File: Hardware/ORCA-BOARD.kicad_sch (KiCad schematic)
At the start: 23 parts, among them J1 USB_C_Receptacle_USB2.0_16P, J3 Screw_Terminal_01x02, SW1 RESET1, SW2 BOOT, U1 D3V3XA4B10LP, U2 ESP32-S3-WROOM-1, U3 AMS1117-3.3, U4 TCA9548APWR

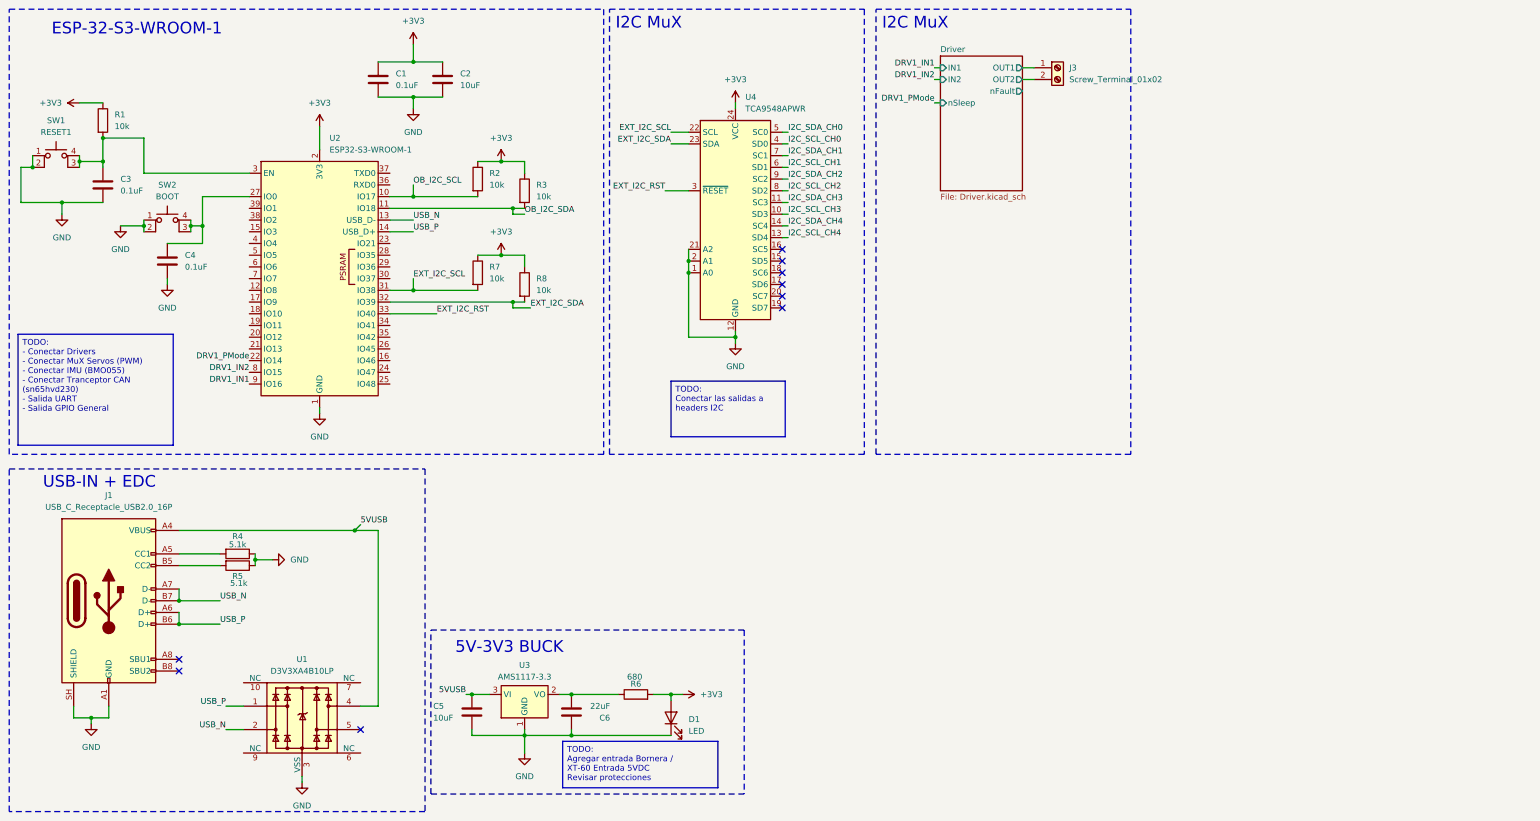
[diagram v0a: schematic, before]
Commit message: Placa de potencia: layout Rev A ruteado y conectado
Buck-boost sincrono de 4 interruptores (LM5175PWPR + 4x PSMN3R2-40YLD) que
entrega 7.2-25 V ajustables a 8 A continuos / 15 A pico desde un pack LiPo
2S-6S, para alimentar los 4 DRV8874.

Layout
- 4 capas, 67.0 x 51.4 mm, 47 componentes, 32 redes, todo SMD en F.Cu
- Ruteo completo: 0 unconnected items
- Corriente de potencia por planos: VBUS, VOUT, VOUT_PRE, SW1 y SW2 con pour
  en F.Cu + In1 + In2 en vez de pistas anchas
- 132 vias de cosido: 16 en SW1, 16 en SW2, 21 en VOUT, 19 en VBUS, 13 en
  VOUT_PRE. Dimensionadas por cantidad, no por tamano
- Vias 0.4/0.3 mm, piso de fabricacion de JLCPCB (recomendacion de Jorge
  Montes). min_via_annular_width ajustado de 0.1 a 0.05 mm para reflejar la
  capacidad real de la fabrica en vez de una regla heredada
- Plano de GND en In1 a 0.1 mm bajo la etapa de potencia, GND y GNDA
  separadas con punto unico de union en R15 (jumper 0 ohm)
- Escape fino (neck-down 0.08 mm) en los pines de U1 donde el paso de
  0.65 mm no admite el clearance de la netclass vecina

Correcciones de netlist
- CS_P/CS_N: el renombrado parcial del lado de U1 dejaba redes de un solo pad
  y el sensado de corriente fisicamente desconectado
- D1: la cadena de bias VBUS -> D1 -> R1 -> VIN colgaba de VCC, que U1 genera
  a partir de VIN. Lazo cerrado sin fuente

Se elimina Hardware/Driver.kicad_sch: el subsheet de drivers pertenece a la
placa logica y el esquematico de potencia ya no lo referencia.

Pendiente antes de fabricar
- Re-exportar Gerbers (los versionados aqui son del 24-sep y no reflejan
  este trabajo)
- Correr DRC sobre esta version y habilitar el parity check con el esquematico
- Verificar la polaridad de ISNS contra el datasheet
- Confirmar continuidad del plano de GND en In1 bajo el lazo de potencia

Detalle completo en Hardware/ORCA-BOARD_Handoff_Ruteo_Manual.md y en
docs/ORCA-Potencia_Dossier_Buck-Boost.md

Co-Authored-By: Claude Opus 5 <noreply@anthropic.com>
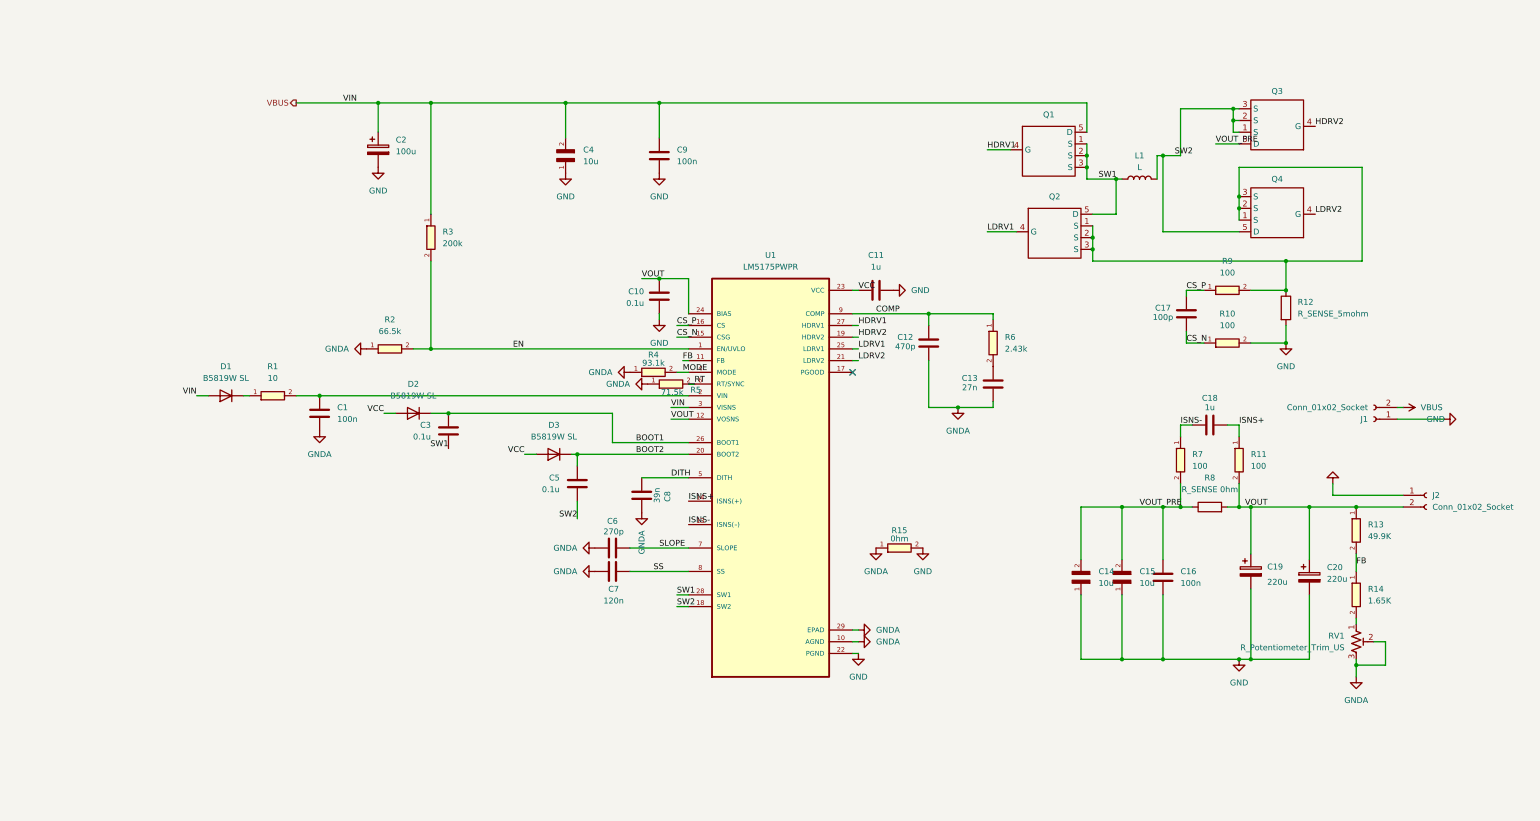
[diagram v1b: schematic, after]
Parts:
- removed C2: 10uF, Capacitor_SMD:C_1206_3216Metric_Pad1.33x1.80mm_HandSolder, symbol Device:C
- removed C4: 0.1uF, Capacitor_SMD:C_0603_1608Metric_Pad1.08x0.95mm_HandSolder, symbol Device:C
- removed D1: LED, LED_SMD:LED_0603_1608Metric_Pad1.05x0.95mm_HandSolder, symbol Device:LED
- removed J1: USB_C_Receptacle_USB2.0_16P, symbol Connector:USB_C_Receptacle_USB2.0_16P
- removed J3: Screw_Terminal_01x02, symbol Connector:Screw_Terminal_01x02
- removed R1, R2, R3, R7: 10k, LED_SMD:LED_0603_1608Metric_Pad1.05x0.95mm_HandSolder, symbol Device:R
- removed R4, R5: 5.1k, LED_SMD:LED_0603_1608Metric_Pad1.05x0.95mm_HandSolder, symbol Device:R
- removed R6: 680, LED_SMD:LED_0603_1608Metric_Pad1.05x0.95mm_HandSolder, symbol Device:R
- removed SW1: RESET1, Button_Switch_SMD:SW_MEC_5GSH9, symbol Switch:SW_MEC_5E
- removed SW2: BOOT, Button_Switch_SMD:SW_MEC_5GSH9, symbol Switch:SW_MEC_5E
- removed U1: D3V3XA4B10LP, Package_DFN_QFN:Diodes_UDFN-10_1x2.5mm_P0.5mm, symbol Power_Protection:D3V3XA4B10LP
- removed U2: ESP32-S3-WROOM-1, RF_Module:ESP32-S3-WROOM-1, symbol RF_Module:ESP32-S3-WROOM-1
- removed U3: AMS1117-3.3, Package_TO_SOT_SMD:SOT-223-3_TabPin2, symbol Regulator_Linear:AMS1117-3.3
- removed U4: TCA9548APWR, Package_SO:TSSOP-24_4.4x7.8mm_P0.65mm, symbol Interface_Expansion:TCA9548APWR
- added C10: 0.1u, RC0603FR-1375RL:0603, symbol Device:C
- added C11, C18: 1u, C0805X105K8RAC7210:CAPC2012X100N, symbol Device:C
- added C12: 470p, RC0603FR-1375RL:0603, symbol Device:C
- added C13: 27n, RC0603FR-1375RL:0603, symbol Device:C
- added C14, C15, C4: 10u, CGA6P1X7R1E106M250AC:CAPC3225X280N, symbol CGA6P1X7R1E106M250AC:CGA6P1X7R1E106M250AC
- added C16, C9: 100n, CGA6P1X7R1E106M250AC:CAPC3225X280N, symbol Device:C
- added C17: 100p, RC0603FR-1375RL:0603, symbol Device:C
- added C19, C20: 220u, Capacitor_THT:CP_Radial_D8.0mm_P3.50mm, symbol Device:C_Polarized
- added C2: 100u, Capacitor_THT:CP_Radial_D8.0mm_P3.50mm, symbol Device:C_Polarized
- added C7: 120n, RC0603FR-1375RL:0603, symbol Device:C
- added C8: 39n, RC0603FR-1375RL:0603, symbol Device:C
- added D1, D2, D3: B5819W SL, Diode_SMD:D_SOD-123, symbol Diode:1N4448W
- added J1, J2: Conn_01x02_Socket, Connector_AMASS:AMASS_XT60-F_1x02_P7.20mm_Vertical, symbol Connector:Conn_01x02_Socket
- added L1: L, ORCAVO:L_Pulse_PA4344, symbol Device:L
- added Q1, Q2, Q3, Q4: (no value), Package_TO_SOT_SMD:LFPAK56, symbol LM5175PWPR:PSMN3R2-40YLD
- added R1: 10, RC0603FR-1375RL:0603, symbol RC0603FR-1375RL:R_0603
- added R10, R11, R7, R9: 100, RC0603FR-1375RL:0603, symbol RC0603FR-1375RL:R_0603
- added R12: R_SENSE_5mohm, ORCAVO:R_2512_Kelvin_TLRP, symbol Device:R
- added R13: 49.9K, RC0603FR-1375RL:0603, symbol RC0603FR-1375RL:R_0603
- added R14: 1.65K, RC0603FR-1375RL:0603, symbol RC0603FR-1375RL:R_0603
- added R15: 0hm, RC0603FR-1375RL:0603, symbol RC0603FR-1375RL:R_0603
- added R2: 66.5k, RC0603FR-1375RL:0603, symbol RC0603FR-1375RL:R_0603
- added R3: 200k, RC0603FR-1375RL:0603, symbol RC0603FR-1375RL:R_0603
- added R4: 93.1k, RC0603FR-1375RL:0603, symbol RC0603FR-1375RL:R_0603
- added R5: 71.5k, RC0603FR-1375RL:0603, symbol RC0603FR-1375RL:R_0603
- added R6: 2.43k, RC0603FR-1375RL:0603, symbol RC0603FR-1375RL:R_0603
- added RV1: R_Potentiometer_Trim_US, Potentiometer_THT:Potentiometer_Bourns_3296W_Vertical, symbol Device:R_Potentiometer_Trim_US
- added U1: LM5175PWPR, ORCAVO:LM5175PWP, symbol LM5175PWPR:LM5175PWPR
- C1: value 0.1uF -> 100n; footprint Capacitor_SMD:C_0603_1608Metric_Pad1.08x0.95mm_HandSolder -> RC0603FR-1375RL:0603
- C3: value 0.1uF -> 0.1u; footprint Capacitor_SMD:C_0603_1608Metric_Pad1.08x0.95mm_HandSolder -> RC0603FR-1375RL:0603
- C5: value 10uF -> 0.1u; footprint Capacitor_SMD:C_1206_3216Metric_Pad1.33x1.80mm_HandSolder -> RC0603FR-1375RL:0603
- C6: value 22uF -> 270p; footprint Capacitor_SMD:C_1206_3216Metric_Pad1.33x1.80mm_HandSolder -> RC0603FR-1375RL:0603
- R8: value 10k -> R_SENSE 0hm; footprint LED_SMD:LED_0603_1608Metric_Pad1.05x0.95mm_HandSolder -> 2512_RSENSE:RES_1-2176421-2
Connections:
- net GND: now also C10.2, C11.2, C14.1, C15.1, C16.2, C19.2, C2.2, C20.2, C4.1, C9.2, J1.1 (Pin_1), J2.1 (Pin_1), R10.2, R12.2, R15.2, U1.22 (PGND); no longer C1.2, C3.2, C5.2, C6.1
- net BOOT1: now reaches C3.1
- net BOOT1: now also D2.1 (K), U1.26 (BOOT1)
- net SLOPE: now reaches C6.2
- net SLOPE: now also U1.7 (SLOPE)
- net +3V3: no longer names the net of C1.1
- net +3V3: now also R1.2, U1.2 (VIN); no longer R8.1
- net 5VUSB renamed BOOT2
- net BOOT2: now also D3.1 (K), U1.20 (BOOT2)
- net EXT_I2C_SDA renamed VOUT
- net VOUT: now also C10.1, C19.1, C20.1, J2.2 (Pin_2), R11.2, R13.1, U1.12 (VOSNS), U1.24 (BIAS)
- new net: C13.2, R6.2
- new net: R14.2, RV1.1
- new net: D1.1 (K), R1.1
- new net: Q2.1 (S), Q2.2 (S), Q2.3 (S), Q4.1 (S), Q4.2 (S), Q4.3 (S), R12.1, R9.2
- new net COMP: C12.2, R6.1, U1.9 (COMP)
- new net CS_N: C17.1, R10.1, U1.15 (CSG)
- new net CS_P: C17.2, R9.1, U1.16 (CS)
- new net DITH: C8.2, U1.5 (DITH)
- new net EN: R2.2, R3.2, U1.1 (EN/UVLO)
- new net FB: R13.2, R14.1, U1.11 (FB)
- new net GNDA: C1.2, C12.1, C13.1, C6.1, C7.1, C8.1, R15.1, R2.1, R4.1, R5.1, RV1.2, RV1.3, U1.10 (AGND), U1.29 (EPAD)
- new net HDRV1: Q1.4 (G), U1.27 (HDRV1)
- new net HDRV2: Q3.4 (G), U1.19 (HDRV2)
- new net ISNS+: C18.2, R11.1, U1.14 (ISNS(+))
- new net ISNS-: C18.1, R7.1, U1.13 (ISNS(–))
- new net LDRV1: Q2.4 (G), U1.25 (LDRV1)
- new net LDRV2: Q4.4 (G), U1.21 (LDRV2)
- new net MODE: R4.2, U1.4 (MODE)
- new net RT: R5.2, U1.6 (RT/SYNC)
- new net SS: C7.2, U1.8 (SS)
- new net SW1: C3.2, L1.1, Q1.1 (S), Q1.2 (S), Q1.3 (S), Q2.5 (D), U1.28 (SW1)
- new net SW2: C5.2, L1.2, Q3.1 (S), Q3.2 (S), Q3.3 (S), Q4.5 (D), U1.18 (SW2)
- new net VBUS: C2.1, C4.2, C9.1, D1.2 (A), J1.2 (Pin_2), Q1.5 (D), R3.1, U1.3 (VISNS)
- new net VCC: C11.1, D2.2 (A), D3.2 (A), U1.23 (VCC)
- new net VOUT_PRE: C14.2, C15.2, C16.1, Q3.5 (D), R7.2, R8.1
- no-connect marks 9 -> 1
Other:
- removed sheet Driver
- note removed: "5V-3V3 BUCK"
- note removed: "ESP-32-S3-WROOM-1"
- note removed: "I2C MuX"
- note removed: "USB-IN + EDC"
- company: (none) -> L.A.A, J.F.A, F.G
- title: (none) -> ORCA BOARD
